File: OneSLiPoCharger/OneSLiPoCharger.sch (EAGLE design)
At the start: 55 parts, among them IC1 LM358N, Q1 BUZ10

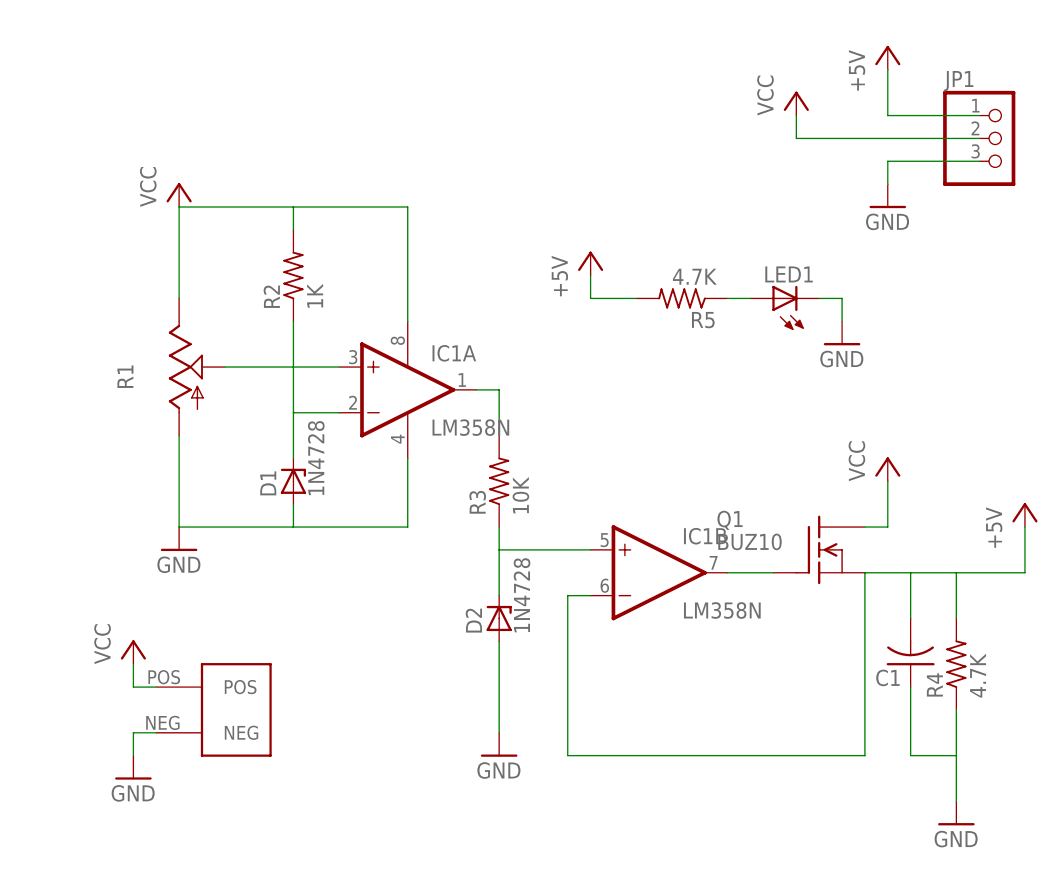
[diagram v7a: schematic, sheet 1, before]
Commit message: Fix miswired input on first opamp. Add a positive feedback volage divider for some hysteresis.
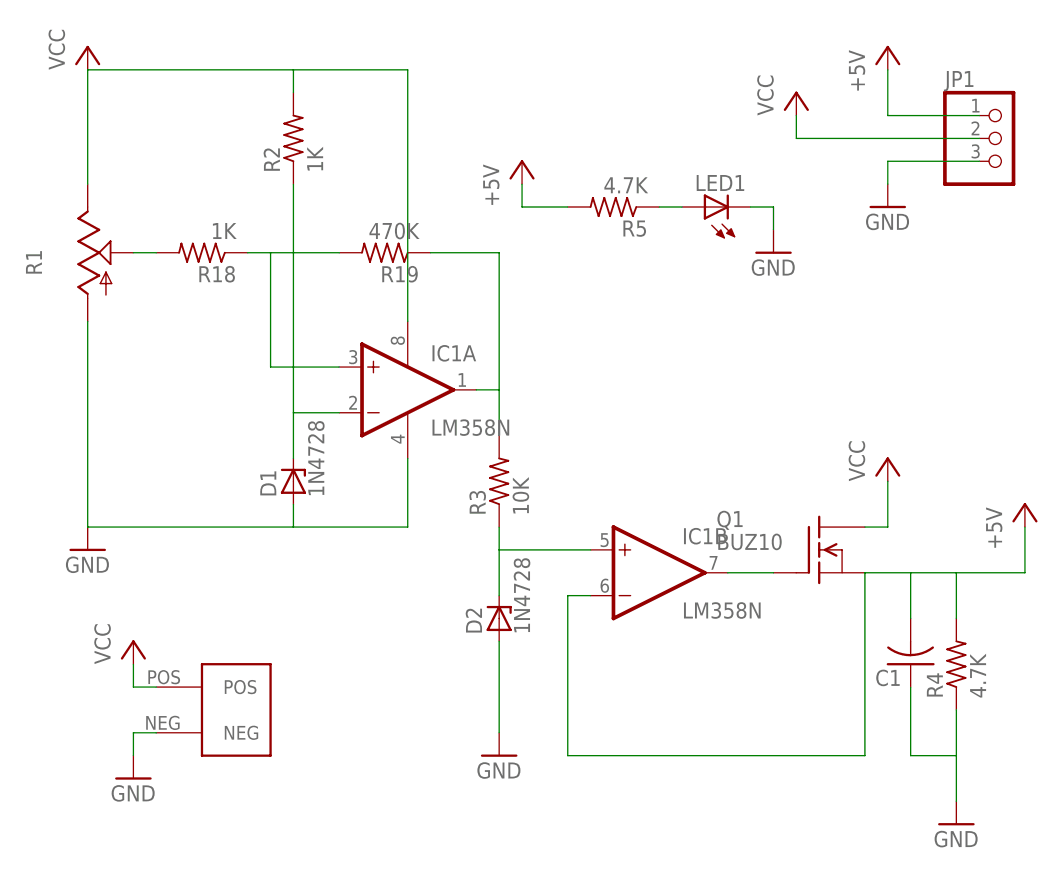
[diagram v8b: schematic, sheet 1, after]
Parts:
- added R18: 1K, rcl:R-US_0207/10
- added R19: 470K, rcl:R-US_0207/10
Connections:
- new net N$31: IC1A.+IN, R18.1, R19.2
- net N$1: now also R18.2; no longer IC1A.+IN
- net N$4: now also R19.1
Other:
- moved on the sheet: LED1, R1, R2, R5
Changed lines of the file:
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@@
 <part name="P+12" library="supply1" deviceset="+5V" device=""/>
 <part name="P+13" library="supply1" deviceset="VCC" device=""/>
+<part name="R18" library="rcl" deviceset="R-US_" device="0207/10" value="1K"/>
+<part name="R19" library="rcl" deviceset="R-US_" device="0207/10" value="470K"/>
 </parts>
 <sheets>
@@
 </plain>
 <instances>
-<instance part="R1" gate="G$1" x="22.86" y="43.18"/>
+<instance part="R1" gate="G$1" x="12.7" y="55.88"/>
 <instance part="IC1" gate="A" x="48.26" y="40.64"/>
 <instance part="IC1" gate="B" x="76.2" y="20.32"/>
-<instance part="P+1" gate="VCC" x="22.86" y="63.5"/>
-<instance part="GND1" gate="1" x="22.86" y="22.86"/>
+<instance part="P+1" gate="VCC" x="12.7" y="78.74"/>
+<instance part="GND1" gate="1" x="12.7" y="22.86"/>
 <instance part="D1" gate="1" x="35.56" y="30.48" rot="R90"/>
-<instance part="R2" gate="G$1" x="35.56" y="53.34" rot="R90"/>
+<instance part="R2" gate="G$1" x="35.56" y="68.58" rot="R90"/>
 <instance part="IC1" gate="P" x="48.26" y="40.64"/>
 <instance part="D2" gate="1" x="58.42" y="15.24" rot="R90"/>
@@
 <instance part="GND7" gate="1" x="17.78" y="-2.54"/>
 <instance part="P+5" gate="VCC" x="17.78" y="12.7"/>
-<instance part="LED1" gate="G$1" x="88.9" y="50.8" rot="R90"/>
-<instance part="R5" gate="G$1" x="78.74" y="50.8" rot="R180"/>
-<instance part="P+6" gate="1" x="68.58" y="55.88"/>
-<instance part="GND8" gate="1" x="96.52" y="45.72"/>
+<instance part="LED1" gate="G$1" x="81.28" y="60.96" rot="R90"/>
+<instance part="R5" gate="G$1" x="71.12" y="60.96" rot="R180"/>
+<instance part="P+6" gate="1" x="60.96" y="66.04"/>
+<instance part="GND8" gate="1" x="88.9" y="55.88"/>
 <instance part="JP1" gate="A" x="114.3" y="68.58"/>
 <instance part="GND24" gate="1" x="101.6" y="60.96"/>
 <instance part="P+12" gate="1" x="101.6" y="78.74"/>
 <instance part="P+13" gate="VCC" x="91.44" y="73.66"/>
+<instance part="R18" gate="G$1" x="25.4" y="55.88" rot="R180"/>
+<instance part="R19" gate="G$1" x="45.72" y="55.88" rot="R180"/>
 </instances>
 <busses>
@@
 <segment>
 <pinref part="D1" gate="1" pin="C"/>
-<wire x1="35.56" y1="48.26" x2="35.56" y2="38.1" width="0.1524" layer="91"/>
+<wire x1="35.56" y1="63.5" x2="35.56" y2="38.1" width="0.1524" layer="91"/>
 <pinref part="R2" gate="G$1" pin="1"/>
 <pinref part="IC1" gate="A" pin="-IN"/>
@@
 <pinref part="P+1" gate="VCC" pin="VCC"/>
 <pinref part="R1" gate="G$1" pin="E"/>
-<wire x1="22.86" y1="60.96" x2="22.86" y2="50.8" width="0.1524" layer="91"/>
+<wire x1="12.7" y1="76.2" x2="12.7" y2="63.5" width="0.1524" layer="91"/>
 <pinref part="R2" gate="G$1" pin="2"/>
-<wire x1="22.86" y1="60.96" x2="35.56" y2="60.96" width="0.1524" layer="91"/>
-<wire x1="35.56" y1="60.96" x2="35.56" y2="58.42" width="0.1524" layer="91"/>
+<wire x1="12.7" y1="76.2" x2="35.56" y2="76.2" width="0.1524" layer="91"/>
+<wire x1="35.56" y1="76.2" x2="35.56" y2="73.66" width="0.1524" layer="91"/>
 <pinref part="IC1" gate="P" pin="V+"/>
-<wire x1="35.56" y1="60.96" x2="48.26" y2="60.96" width="0.1524" layer="91"/>
-<wire x1="48.26" y1="60.96" x2="48.26" y2="48.26" width="0.1524" layer="91"/>
+<wire x1="35.56" y1="76.2" x2="48.26" y2="76.2" width="0.1524" layer="91"/>
+<wire x1="48.26" y1="76.2" x2="48.26" y2="48.26" width="0.1524" layer="91"/>
 </segment>
 <segment>
@@
 <pinref part="R1" gate="G$1" pin="A"/>
 <pinref part="GND1" gate="1" pin="GND"/>
-<wire x1="22.86" y1="35.56" x2="22.86" y2="25.4" width="0.1524" layer="91"/>
+<wire x1="12.7" y1="48.26" x2="12.7" y2="25.4" width="0.1524" layer="91"/>
 <pinref part="D1" gate="1" pin="A"/>
-<wire x1="22.86" y1="25.4" x2="35.56" y2="25.4" width="0.1524" layer="91"/>
+<wire x1="12.7" y1="25.4" x2="35.56" y2="25.4" width="0.1524" layer="91"/>
 <wire x1="35.56" y1="25.4" x2="35.56" y2="27.94" width="0.1524" layer="91"/>
 <pinref part="IC1" gate="P" pin="V-"/>
@@
 <pinref part="LED1" gate="G$1" pin="C"/>
 <pinref part="GND8" gate="1" pin="GND"/>
-<wire x1="93.98" y1="50.8" x2="96.52" y2="50.8" width="0.1524" layer="91"/>
-<wire x1="96.52" y1="50.8" x2="96.52" y2="48.26" width="0.1524" layer="91"/>
+<wire x1="86.36" y1="60.96" x2="88.9" y2="60.96" width="0.1524" layer="91"/>
+<wire x1="88.9" y1="60.96" x2="88.9" y2="58.42" width="0.1524" layer="91"/>
 </segment>
 <segment>
@@
 <wire x1="111.76" y1="66.04" x2="101.6" y2="66.04" width="0.1524" layer="91"/>
 <wire x1="101.6" y1="66.04" x2="101.6" y2="63.5" width="0.1524" layer="91"/>
-</segment>
-</net>
-<net name="N$1" class="0">
-<segment>
-<pinref part="R1" gate="G$1" pin="S"/>
-<pinref part="IC1" gate="A" pin="+IN"/>
-<wire x1="27.94" y1="43.18" x2="40.64" y2="43.18" width="0.1524" layer="91"/>
 </segment>
 </net>
@@
 <wire x1="55.88" y1="40.64" x2="58.42" y2="40.64" width="0.1524" layer="91"/>
 <wire x1="58.42" y1="40.64" x2="58.42" y2="35.56" width="0.1524" layer="91"/>
+<pinref part="R19" gate="G$1" pin="1"/>
+<wire x1="50.8" y1="55.88" x2="58.42" y2="55.88" width="0.1524" layer="91"/>
+<wire x1="58.42" y1="55.88" x2="58.42" y2="40.64" width="0.1524" layer="91"/>
 </segment>
 </net>
@@
 <pinref part="P+6" gate="1" pin="+5V"/>
 <pinref part="R5" gate="G$1" pin="2"/>
-<wire x1="68.58" y1="53.34" x2="68.58" y2="50.8" width="0.1524" layer="91"/>
-<wire x1="68.58" y1="50.8" x2="73.66" y2="50.8" width="0.1524" layer="91"/>
+<wire x1="60.96" y1="63.5" x2="60.96" y2="60.96" width="0.1524" layer="91"/>
+<wire x1="60.96" y1="60.96" x2="66.04" y2="60.96" width="0.1524" layer="91"/>
 </segment>
 <segment>
@@
 <pinref part="R5" gate="G$1" pin="1"/>
 <pinref part="LED1" gate="G$1" pin="A"/>
-<wire x1="83.82" y1="50.8" x2="86.36" y2="50.8" width="0.1524" layer="91"/>
-</segment>
-</net>
+<wire x1="76.2" y1="60.96" x2="78.74" y2="60.96" width="0.1524" layer="91"/>
+</segment>
+</net>
+<net name="N$1" class="0">
+<segment>
+<pinref part="R1" gate="G$1" pin="S"/>
+<pinref part="R18" gate="G$1" pin="2"/>
+<wire x1="17.78" y1="55.88" x2="20.32" y2="55.88" width="0.1524" layer="91"/>
+</segment>
+</net>
+<net name="N$31" class="0">
+<segment>
+<pinref part="R18" gate="G$1" pin="1"/>
+<pinref part="R19" gate="G$1" pin="2"/>
+<wire x1="30.48" y1="55.88" x2="33.02" y2="55.88" width="0.1524" layer="91"/>
+<wire x1="33.02" y1="55.88" x2="40.64" y2="55.88" width="0.1524" layer="91"/>
+<wire x1="33.02" y1="55.88" x2="33.02" y2="43.18" width="0.1524" layer="91"/>
+<pinref part="IC1" gate="A" pin="+IN"/>
+<wire x1="33.02" y1="43.18" x2="40.64" y2="43.18" width="0.1524" layer="91"/>
+</segment>
+</net>
